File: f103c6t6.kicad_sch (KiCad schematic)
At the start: 11 parts, among them J1 Conn_01x03_Pin, J2 Conn_01x04_Pin, J3 Conn_01x02_Pin, J4 Conn_01x10_Pin, J5 Conn_01x06_Pin, U1 STM32F103C6Tx, U2 AMS1117-3.3

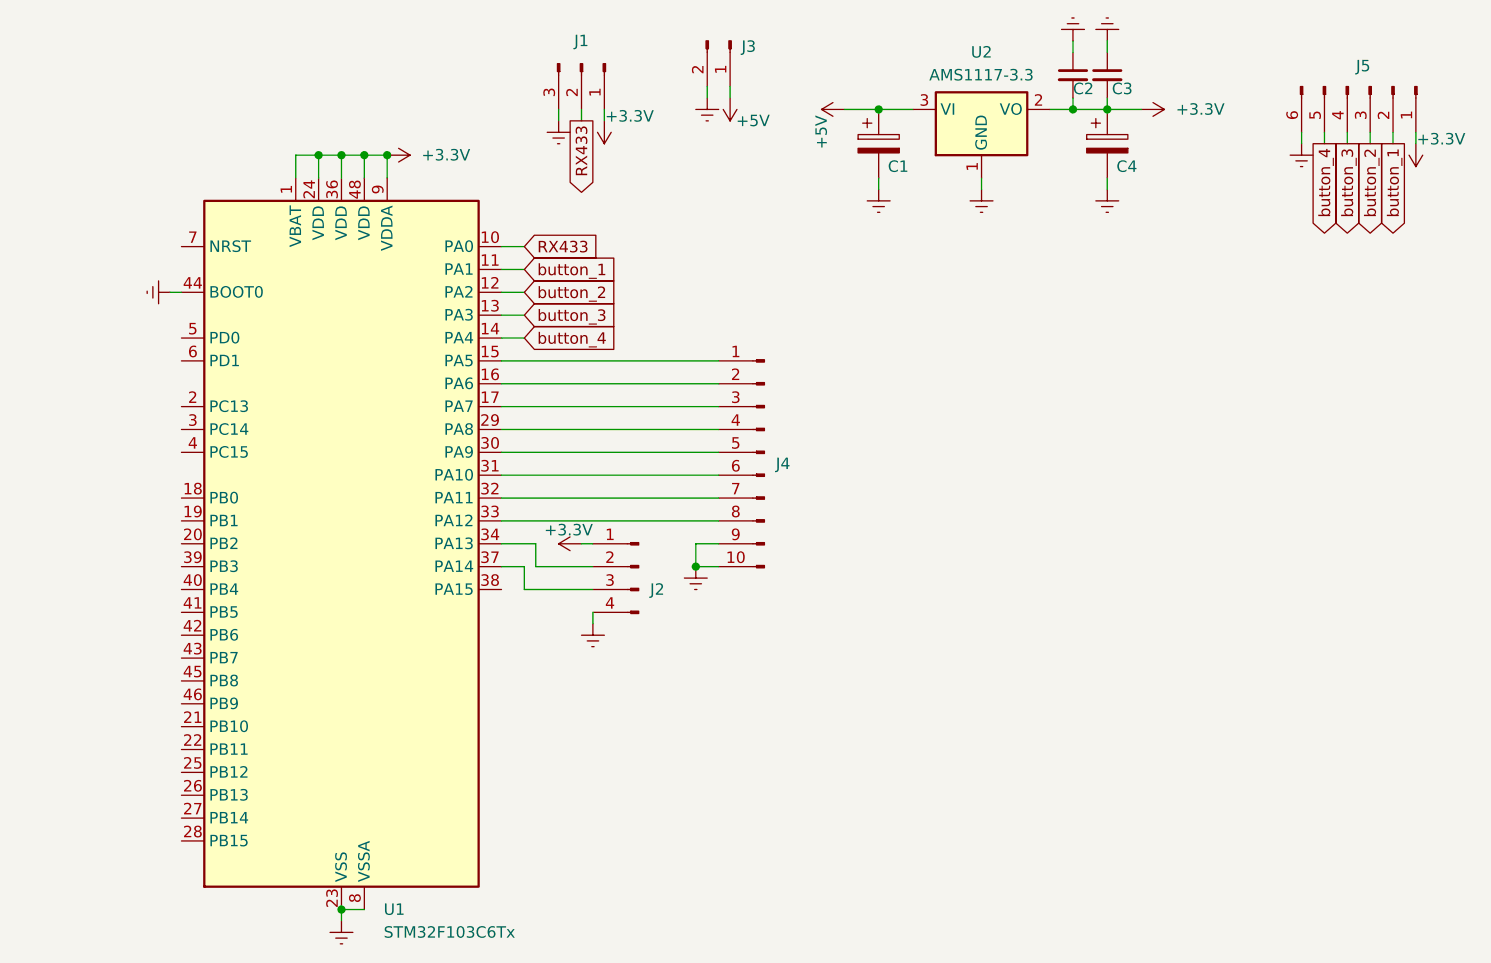
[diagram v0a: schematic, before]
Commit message: serial +
Добавлен сериал порт для монитора ардуино
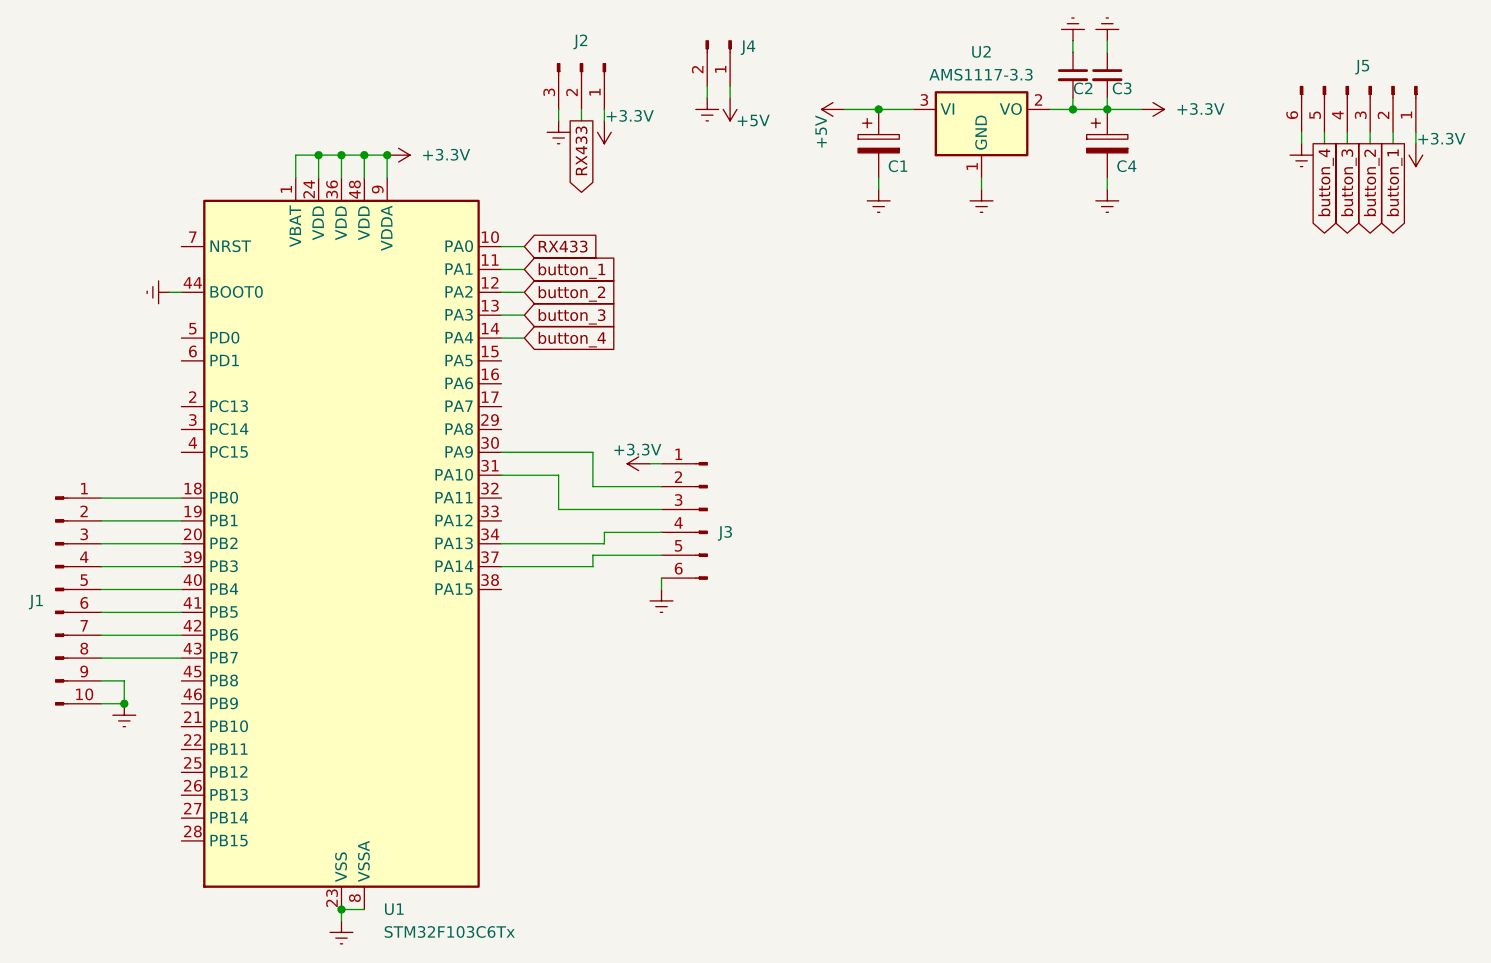
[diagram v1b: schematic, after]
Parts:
- removed J2: Conn_01x04_Pin, main:PinHeader_1x04_P2.54mm_Vertical, symbol Connector:Conn_01x04_Pin
- removed J4: Conn_01x10_Pin, main:PinHeader_2x05_P2.54mm_Vertical, symbol Connector:Conn_01x10_Pin
- added J1: Conn_01x10_Pin, main:PinHeader_2x05_P2.54mm_Vertical, symbol Connector:Conn_01x10_Pin
- added J3: Conn_01x06_Pin, main:PinHeader_1x06_P2.54mm_Vertical, symbol Connector:Conn_01x06_Pin
- renumbered J1 to J2, J3 to J4
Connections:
- net +3.3V: now also J3.1 (Pin_1)
- net GNDREF: now also J1.10 (Pin_10), J1.9 (Pin_9), J3.6 (Pin_6)
- net at U1.30 (PA9): now also J3.2 (Pin_2)
- net at U1.31 (PA10): now also J3.3 (Pin_3)
- net at U1.18 (PB0): now also J1.1 (Pin_1)
- net at U1.19 (PB1): now also J1.2 (Pin_2)
- net at U1.20 (PB2): now also J1.3 (Pin_3)
- net at U1.34 (PA13): now also J3.4 (Pin_4)
- net at U1.37 (PA14): now also J3.5 (Pin_5)
- net at U1.39 (PB3): now also J1.4 (Pin_4)
- net at U1.40 (PB4): now also J1.5 (Pin_5)
- net at U1.41 (PB5): now also J1.6 (Pin_6)
- net at U1.42 (PB6): now also J1.7 (Pin_7)
- net at U1.43 (PB7): now also J1.8 (Pin_8)

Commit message: Оптимизация
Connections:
- net TX: now reaches J3.2 (Pin_2), U1.30 (PA9)
- net RX: now reaches J3.3 (Pin_3), U1.31 (PA10)
- net SWDIO: now reaches J3.4 (Pin_4), U1.34 (PA13)
- net SWCLK: now reaches J3.5 (Pin_5), U1.37 (PA14)
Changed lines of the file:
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@@
+		)
+	)
+	(label "RX"
+		(at 116.84 81.28 0)
+		(effects
+			(font
+				(size 1.27 1.27)
+			)
+			(justify left bottom)
+		)
+	)
+	(label "SWDIO"
+		(at 116.84 83.82 0)
+		(effects
+			(font
+				(size 1.27 1.27)
+			)
+			(justify left bottom)
+		)
+	)
+	(label "SWCLK"
+		(at 116.84 86.36 0)
+		(effects
+			(font
+				(size 1.27 1.27)
+			)
+			(justify left bottom)
+		)
+	)
+	(label "TX"
+		(at 116.84 78.74 0)
+		(effects
+			(font
+				(size 1.27 1.27)
+			)
+			(justify left bottom)
 		)
 	)
